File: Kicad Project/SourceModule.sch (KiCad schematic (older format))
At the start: 0 parts

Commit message: Damian edits
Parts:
- added MS?: PowerDivider, symbol PowerDivider
- added U?: RMK-3-93+, symbol RMK-3-93+
- added VCO?: MAX2752, symbol MAX2752
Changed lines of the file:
@@
 $Descr A4 11693 8268
 encoding utf-8
-Sheet 2 3
+Sheet 2 4
 Title ""
 Date ""
@@
 Comment4 ""
 $EndDescr
+$Comp
+L MAX2752 VCO?
+U 1 1 59F141B1
+P 3700 2450
+F 0 "VCO?" H 4100 3000 60  0000 C CNN
+F 1 "MAX2752" H 3400 3000 60  0000 C CNN
+F 2 "" H 3700 2450 60  0001 C CNN
+F 3 "" H 3700 2450 60  0001 C CNN
+	1    3700 2450
+	1    0    0    -1
+$EndComp
+$Comp
+L RMK-3-93+ U?
+U 1 1 59F14344
+P 5750 2250
+F 0 "U?" H 6190 2820 60  0000 C CNN
+F 1 "RMK-3-93+" H 5520 2820 60  0000 C CNN
+F 2 "" H 5750 2250 60  0001 C CNN
+F 3 "" H 5750 2250 60  0001 C CNN
+	1    5750 2250
+	1    0    0    -1
+$EndComp
+$Comp
+L PowerDivider MS?
+U 1 1 59F143BD
+P 7600 2250
+F 0 "MS?" H 8010 2800 60  0000 C CNN
+F 1 "PowerDivider" H 7390 2800 60  0000 C CNN
+F 2 "" H 7600 2250 60  0001 C CNN
+F 3 "" H 7600 2250 60  0001 C CNN
+	1    7600 2250
+	1    0    0    -1
+$EndComp
 $EndSCHEMATC

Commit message: Component Library linked Circuit work on Source Module
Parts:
- added C? (x2): 220pF, symbol C
- added C?: .1uF, symbol C
- added C?: C, symbol C
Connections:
- net labels added: +3.3V, GND
- wire segments 0 -> 22
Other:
- note added: "-3dBm"
- note added: "0dBm\n"
- note added: "Amplifier"
- note added: "Frequency Feedback"
- note added: "Frequency Multiplier"
- note added: "Power Splitter"
- note added: "Teensy Interface"
- note added: "To Premp\nFrequency Multiplier"
- note added: "To TX/RX multiplier"
- note added: "Voltage Controlled Oscillator\n"
- moved on the sheet: MS?, U?, VCO?
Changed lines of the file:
@@
 LIBS:contrib
 LIBS:valves
+LIBS:RadarProject
 LIBS:Radar-cache
 EELAYER 25 0
@@
 L MAX2752 VCO?
 U 1 1 59F141B1
-P 3700 2450
-F 0 "VCO?" H 4100 3000 60  0000 C CNN
-F 1 "MAX2752" H 3400 3000 60  0000 C CNN
-F 2 "" H 3700 2450 60  0001 C CNN
-F 3 "" H 3700 2450 60  0001 C CNN
-	1    3700 2450
+P 2900 2450
+F 0 "VCO?" H 3300 3000 60  0000 C CNN
+F 1 "MAX2752" H 2600 3000 60  0000 C CNN
+F 2 "" H 2900 2450 60  0001 C CNN
+F 3 "" H 2900 2450 60  0001 C CNN
+	1    2900 2450
 	1    0    0    -1
 $EndComp
@@
 L RMK-3-93+ U?
 U 1 1 59F14344
-P 5750 2250
-F 0 "U?" H 6190 2820 60  0000 C CNN
-F 1 "RMK-3-93+" H 5520 2820 60  0000 C CNN
-F 2 "" H 5750 2250 60  0001 C CNN
-F 3 "" H 5750 2250 60  0001 C CNN
-	1    5750 2250
+P 6850 2250
+F 0 "U?" H 7290 2820 60  0000 C CNN
+F 1 "RMK-3-93+" H 6620 2820 60  0000 C CNN
+F 2 "" H 6850 2250 60  0001 C CNN
+F 3 "" H 6850 2250 60  0001 C CNN
+	1    6850 2250
 	1    0    0    -1
 $EndComp
@@
 L PowerDivider MS?
 U 1 1 59F143BD
-P 7600 2250
-F 0 "MS?" H 8010 2800 60  0000 C CNN
-F 1 "PowerDivider" H 7390 2800 60  0000 C CNN
-F 2 "" H 7600 2250 60  0001 C CNN
-F 3 "" H 7600 2250 60  0001 C CNN
-	1    7600 2250
-	1    0    0    -1
-$EndComp
+P 9000 2300
+F 0 "MS?" H 9410 2850 60  0000 C CNN
+F 1 "PowerDivider" H 8790 2850 60  0000 C CNN
+F 2 "" H 9000 2300 60  0001 C CNN
+F 3 "" H 9000 2300 60  0001 C CNN
+	1    9000 2300
+	1    0    0    -1
+$EndComp
+$Comp
+L +3.3V #PWR?
+U 1 1 59F4A689
+P 4100 2600
+F 0 "#PWR?" H 4100 2450 50  0001 C CNN
+F 1 "+3.3V" H 4100 2740 50  0000 C CNN
+F 2 "" H 4100 2600 50  0001 C CNN
+F 3 "" H 4100 2600 50  0001 C CNN
+	1    4100 2600
+	1    0    0    -1
+$EndComp
+Wire Wire Line
+	3600 2650 4100 2650
+Wire Wire Line
+	4100 2650 4300 2650
+Wire Wire Line
+	4100 2850 4100 2650
+Wire Wire Line
+	4100 2650 4100 2600
+Wire Wire Line
+	3600 2850 3900 2850
+Wire Wire Line
+	3900 2850 4100 2850
+Connection ~ 4100 2650
+$Comp
+L C C?
+U 1 1 59F4A7A6
+P 3900 3150
+F 0 "C?" H 3925 3250 50  0000 L CNN
+F 1 "220pF" H 3925 3050 50  0000 L CNN
+F 2 "" H 3938 3000 50  0001 C CNN
+F 3 "" H 3900 3150 50  0001 C CNN
+	1    3900 3150
+	1    0    0    -1
+$EndComp
+$Comp
+L C C?
+U 1 1 59F4A7E2
+P 4300 2850
+F 0 "C?" H 4325 2950 50  0000 L CNN
+F 1 "220pF" H 4325 2750 50  0000 L CNN
+F 2 "" H 4338 2700 50  0001 C CNN
+F 3 "" H 4300 2850 50  0001 C CNN
+	1    4300 2850
+	1    0    0    -1
+$EndComp
+$Comp
+L C C?
+U 1 1 59F4A91F
+P 1750 1700
+F 0 "C?" H 1775 1800 50  0000 L CNN
+F 1 ".1uF" H 1775 1600 50  0000 L CNN
+F 2 "" H 1788 1550 50  0001 C CNN
+F 3 "" H 1750 1700 50  0001 C CNN
+	1    1750 1700
+	1    0    0    -1
+$EndComp
+$Comp
+L GND #PWR?
+U 1 1 59F4A990
+P 1750 1850
+F 0 "#PWR?" H 1750 1600 50  0001 C CNN
+F 1 "GND" H 1750 1700 50  0000 C CNN
+F 2 "" H 1750 1850 50  0001 C CNN
+F 3 "" H 1750 1850 50  0001 C CNN
+	1    1750 1850
+	1    0    0    -1
+$EndComp
+$Comp
+L GND #PWR?
+U 1 1 59F4AA4C
+P 3900 3300
+F 0 "#PWR?" H 3900 3050 50  0001 C CNN
+F 1 "GND" H 3900 3150 50  0000 C CNN
+F 2 "" H 3900 3300 50  0001 C CNN
+F 3 "" H 3900 3300 50  0001 C CNN
+	1    3900 3300
+	1    0    0    -1
+$EndComp
+$Comp
+L GND #PWR?
+U 1 1 59F4AA6C
+P 4300 3000
+F 0 "#PWR?" H 4300 2750 50  0001 C CNN
+F 1 "GND" H 4300 2850 50  0000 C CNN
+F 2 "" H 4300 3000 50  0001 C CNN
+F 3 "" H 4300 3000 50  0001 C CNN
+	1    4300 3000
+	1    0    0    -1
+$EndComp
+Wire Wire Line
+	3900 2850 3900 3000
+Connection ~ 3900 2850
+Wire Wire Line
+	4300 2650 4300 2700
+$Comp
+L GND #PWR?
+U 1 1 59F4AB52
+P 3850 1750
+F 0 "#PWR?" H 3850 1500 50  0001 C CNN
+F 1 "GND" H 3850 1600 50  0000 C CNN
+F 2 "" H 3850 1750 50  0001 C CNN
+F 3 "" H 3850 1750 50  0001 C CNN
+	1    3850 1750
+	1    0    0    -1
+$EndComp
+Wire Wire Line
+	3600 2050 3700 2050
+Wire Wire Line
+	3700 2050 3700 1600
+Wire Wire Line
+	3700 1600 3850 1600
+Wire Wire Line
+	3850 1600 3850 1750
+Wire Wire Line
+	2200 2050 2200 1400
+Wire Wire Line
+	2200 1400 1750 1400
+Wire Wire Line
+	1750 1400 1750 1550
+Wire Wire Line
+	2200 2250 1700 2250
+Wire Wire Line
+	3600 2250 4050 2250
+$Comp
+L C C?
+U 1 1 59F4AD70
+P 4200 2250
+F 0 "C?" H 4225 2350 50  0000 L CNN
+F 1 "C" H 4225 2150 50  0000 L CNN
+F 2 "" H 4238 2100 50  0001 C CNN
+F 3 "" H 4200 2250 50  0001 C CNN
+	1    4200 2250
+	0    1    1    0
+$EndComp
+$Comp
+L GND #PWR?
+U 1 1 59F4AE46
+P 1550 2700
+F 0 "#PWR?" H 1550 2450 50  0001 C CNN
+F 1 "GND" H 1550 2550 50  0000 C CNN
+F 2 "" H 1550 2700 50  0001 C CNN
+F 3 "" H 1550 2700 50  0001 C CNN
+	1    1550 2700
+	1    0    0    -1
+$EndComp
+Wire Wire Line
+	1550 2700 1550 2650
+Wire Wire Line
+	1550 2650 2200 2650
+Text Notes 650  1700 0    60   ~ 0
+Teensy Interface
+Text Notes 2450 1150 0    60   ~ 0
+Voltage Controlled Oscillator\n
+Text Notes 5050 1750 0    60   ~ 0
+Amplifier
+Text Notes 6350 1400 0    60   ~ 0
+Frequency Multiplier
+Text Notes 8600 1600 0    60   ~ 0
+Power Splitter
+Text Notes 9600 2450 0    60   ~ 0
+To Premp\nFrequency Multiplier
+Text Notes 9650 1900 0    60   ~ 0
+To TX/RX multiplier
+Wire Wire Line
+	4350 2250 5150 2250
+Wire Wire Line
+	5150 2250 5150 3700
+Wire Wire Line
+	5150 3700 1700 3700
+Text Notes 1900 3650 0    60   ~ 0
+Frequency Feedback
+$Comp
+L GND #PWR?
+U 1 1 59F4B365
+P 6850 2850
+F 0 "#PWR?" H 6850 2600 50  0001 C CNN
+F 1 "GND" H 6850 2700 50  0000 C CNN
+F 2 "" H 6850 2850 50  0001 C CNN
+F 3 "" H 6850 2850 50  0001 C CNN
+	1    6850 2850
+	1    0    0    -1
+$EndComp
+Text Notes 10700 1600 0    60   ~ 0
+0dBm\n
+Connection ~ 5150 2250
+Text Notes 4450 2200 0    60   ~ 0
+-3dBm
 $EndSCHEMATC

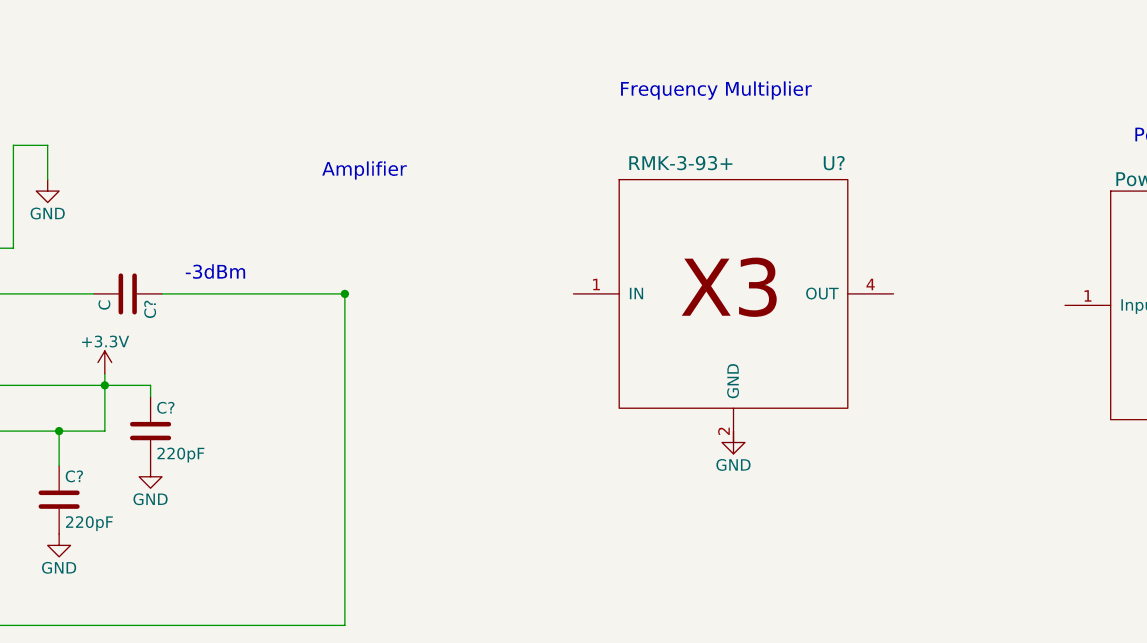
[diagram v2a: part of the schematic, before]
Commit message: Added Power calculations and resistive divider
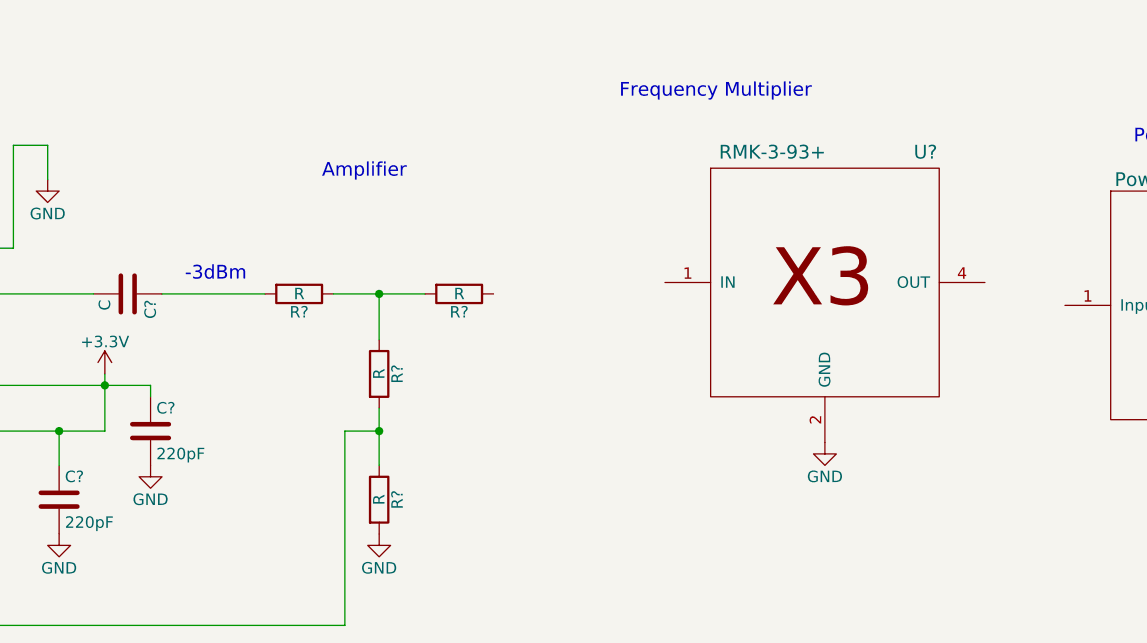
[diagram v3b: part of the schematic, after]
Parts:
- added R? (x4): R, symbol R
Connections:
- wire segments 22 -> 28
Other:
- moved on the sheet: U?
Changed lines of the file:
@@
 L RMK-3-93+ U?
 U 1 1 59F14344
-P 6850 2250
-F 0 "U?" H 7290 2820 60  0000 C CNN
-F 1 "RMK-3-93+" H 6620 2820 60  0000 C CNN
-F 2 "" H 6850 2250 60  0001 C CNN
-F 3 "" H 6850 2250 60  0001 C CNN
-	1    6850 2250
+P 7250 2200
+F 0 "U?" H 7690 2770 60  0000 C CNN
+F 1 "RMK-3-93+" H 7020 2770 60  0000 C CNN
+F 2 "" H 7250 2200 60  0001 C CNN
+F 3 "" H 7250 2200 60  0001 C CNN
+	1    7250 2200
 	1    0    0    -1
 $EndComp
@@
 To TX/RX multiplier
 Wire Wire Line
-	4350 2250 5150 2250
-Wire Wire Line
-	5150 2250 5150 3700
-Wire Wire Line
 	5150 3700 1700 3700
 Text Notes 1900 3650 0    60   ~ 0
@@
 L GND #PWR?
 U 1 1 59F4B365
-P 6850 2850
-F 0 "#PWR?" H 6850 2600 50  0001 C CNN
-F 1 "GND" H 6850 2700 50  0000 C CNN
-F 2 "" H 6850 2850 50  0001 C CNN
-F 3 "" H 6850 2850 50  0001 C CNN
-	1    6850 2850
+P 7250 2900
+F 0 "#PWR?" H 7250 2650 50  0001 C CNN
+F 1 "GND" H 7250 2750 50  0000 C CNN
+F 2 "" H 7250 2900 50  0001 C CNN
+F 3 "" H 7250 2900 50  0001 C CNN
+	1    7250 2900
 	1    0    0    -1
 $EndComp
 Text Notes 10700 1600 0    60   ~ 0
 0dBm\n
-Connection ~ 5150 2250
 Text Notes 4450 2200 0    60   ~ 0
 -3dBm
+$Comp
+L R R?
+U 1 1 59F79D10
+P 4950 2250
+F 0 "R?" V 5030 2250 50  0000 C CNN
+F 1 "R" V 4950 2250 50  0000 C CNN
+F 2 "" V 4880 2250 50  0001 C CNN
+F 3 "" H 4950 2250 50  0001 C CNN
+	1    4950 2250
+	0    1    1    0
+$EndComp
+$Comp
+L R R?
+U 1 1 59F79D75
+P 5300 2600
+F 0 "R?" V 5380 2600 50  0000 C CNN
+F 1 "R" V 5300 2600 50  0000 C CNN
+F 2 "" V 5230 2600 50  0001 C CNN
+F 3 "" H 5300 2600 50  0001 C CNN
+	1    5300 2600
+	1    0    0    -1
+$EndComp
+$Comp
+L R R?
+U 1 1 59F79DA8
+P 5650 2250
+F 0 "R?" V 5730 2250 50  0000 C CNN
+F 1 "R" V 5650 2250 50  0000 C CNN
+F 2 "" V 5580 2250 50  0001 C CNN
+F 3 "" H 5650 2250 50  0001 C CNN
+	1    5650 2250
+	0    1    1    0
+$EndComp
+$Comp
+L R R?
+U 1 1 59F7A0A9
+P 5300 3150
+F 0 "R?" V 5380 3150 50  0000 C CNN
+F 1 "R" V 5300 3150 50  0000 C CNN
+F 2 "" V 5230 3150 50  0001 C CNN
+F 3 "" H 5300 3150 50  0001 C CNN
+	1    5300 3150
+	1    0    0    -1
+$EndComp
+Wire Wire Line
+	5150 2850 5150 3700
+Wire Wire Line
+	5300 2750 5300 2850
+Wire Wire Line
+	5300 2850 5300 3000
+Wire Wire Line
+	5300 2850 5150 2850
+Connection ~ 5300 2850
+$Comp
+L GND #PWR?
+U 1 1 59F7A17E
+P 5300 3300
+F 0 "#PWR?" H 5300 3050 50  0001 C CNN
+F 1 "GND" H 5300 3150 50  0000 C CNN
+F 2 "" H 5300 3300 50  0001 C CNN
+F 3 "" H 5300 3300 50  0001 C CNN
+	1    5300 3300
+	1    0    0    -1
+$EndComp
+Wire Wire Line
+	5100 2250 5300 2250
+Wire Wire Line
+	5300 2250 5500 2250
+Wire Wire Line
+	5300 2450 5300 2250
+Connection ~ 5300 2250
+Wire Wire Line
+	4350 2250 4800 2250
 $EndSCHEMATC

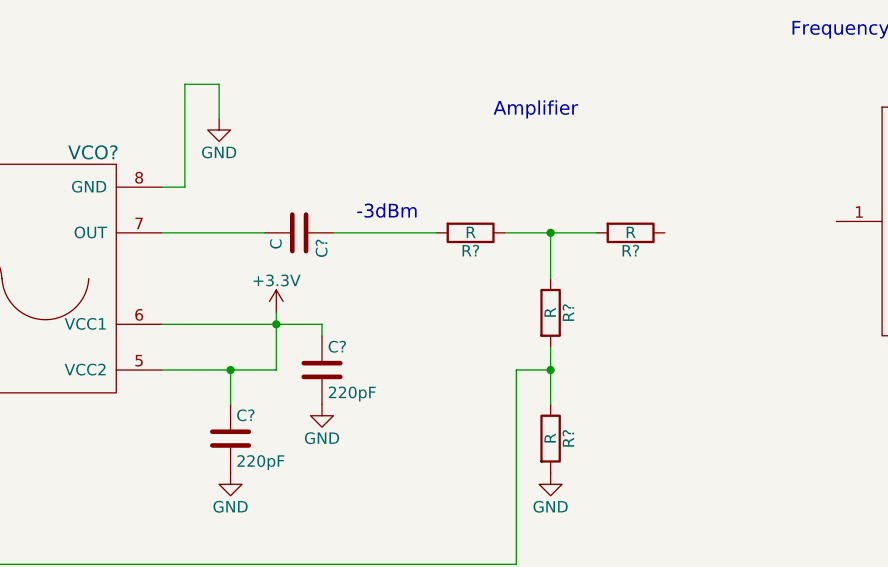
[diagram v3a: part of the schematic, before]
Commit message: Updated labels
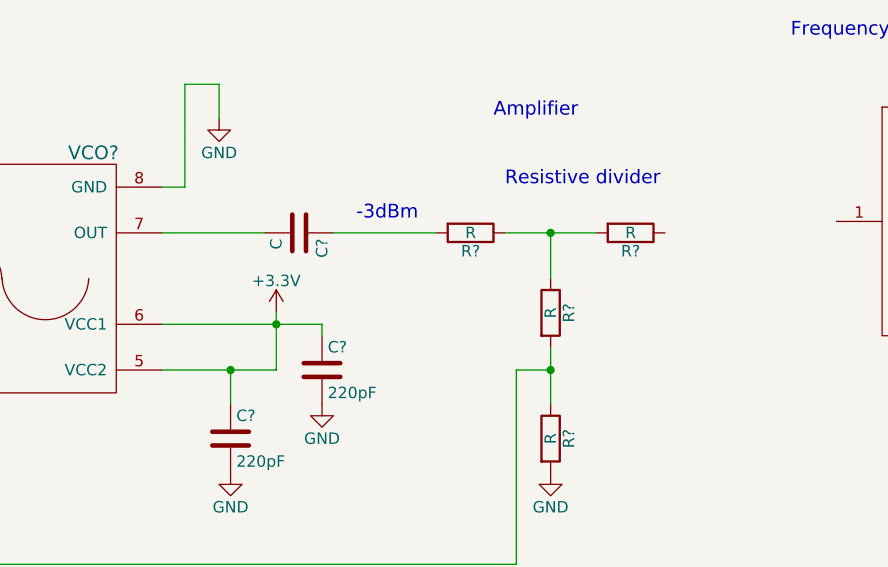
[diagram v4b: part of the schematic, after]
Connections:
- wire segments 28 -> 23
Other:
- note added: "Resistive divider"
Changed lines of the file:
@@
 $EndComp
 Wire Wire Line
-	3600 2650 4100 2650
-Wire Wire Line
-	4100 2650 4300 2650
-Wire Wire Line
-	4100 2850 4100 2650
-Wire Wire Line
-	4100 2650 4100 2600
-Wire Wire Line
-	3600 2850 3900 2850
-Wire Wire Line
-	3900 2850 4100 2850
+	3600 2650 4300 2650
+Wire Wire Line
+	4100 2850 4100 2600
+Wire Wire Line
+	3600 2850 4100 2850
 Connection ~ 4100 2650
 $Comp
@@
 	5150 2850 5150 3700
 Wire Wire Line
-	5300 2750 5300 2850
-Wire Wire Line
-	5300 2850 5300 3000
+	5300 2750 5300 3000
 Wire Wire Line
 	5300 2850 5150 2850
@@
 $EndComp
 Wire Wire Line
-	5100 2250 5300 2250
-Wire Wire Line
-	5300 2250 5500 2250
+	5100 2250 5500 2250
 Wire Wire Line
 	5300 2450 5300 2250
@@
 Wire Wire Line
 	4350 2250 4800 2250
+Text Notes 5100 2050 0    60   ~ 0
+Resistive divider
 $EndSCHEMATC

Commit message: Messed with parts
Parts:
- gave numbers to parts that had none: 1
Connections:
- wire segments 23 -> 24
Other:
- note added: "Teensy Control"
- note removed: "Teensy Interface"
- moved on the sheet: .1uF, C?, MS?, R?, U?, VCO?

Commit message: updates
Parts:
- added .1uF, .1uF? (x2), C? (x2): C, symbol C
- added R? (x4): 75, symbol R
- added U? (x2): GALI-2+, symbol GALI-2+
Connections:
- net labels added: +9V
- wire segments 24 -> 43
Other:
- note added: "4 dBM\n"
- note added: "Filter?\n"
- note added: "lamda/4\n"
- moved on the sheet: .1uF, MS?

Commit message: PCB Changes
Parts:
- .1uF1, .1uF2: renamed from .1uF; footprint (none) -> Capacitors_SMD:C_0603
- .1uF3, .1uF4: renamed from .1uF?; footprint (none) -> Capacitors_SMD:C_0603
- C5, C6, C7, C8, C9: renamed from C?; footprint (none) -> Capacitors_SMD:C_0603
- R10, R11, R12, R13, R14, R7, R8, R9: renamed from R?; footprint (none) -> Resistors_SMD:R_0603
- U6, U8: renamed from U?; footprint (none) -> RadarComponents:Amplifier
- gave numbers to parts that had none: 3

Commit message: PCB and Schematic updates
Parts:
- .1uF1, .1uF2, .1uF3, .1uF4, C5, C6, C7, C8, C9: footprint Capacitors_SMD:C_0603 -> RadarComponents:100PAD
- R10, R11, R12, R13, R14, R7, R8, R9: footprint Resistors_SMD:R_0603 -> RadarComponents:100PAD
- U7: footprint (none) -> RadarComponents:TT1224
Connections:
- net labels added: PowerSplitter
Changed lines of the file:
@@
 F 0 "U7" H 7740 2770 60  0000 C CNN
 F 1 "RMK-3-93+" H 7070 2770 60  0000 C CNN
-F 2 "" H 7300 2200 60  0001 C CNN
+F 2 "RadarComponents:TT1224" H 7300 2200 60  0001 C CNN
 F 3 "" H 7300 2200 60  0001 C CNN
 	1    7300 2200
@@
 F 0 "C6" H 3225 3200 50  0000 L CNN
 F 1 "220pF" H 3225 3000 50  0000 L CNN
-F 2 "Capacitors_SMD:C_0603" H 3238 2950 50  0001 C CNN
+F 2 "RadarComponents:100PAD" H 3238 2950 50  0001 C CNN
 F 3 "" H 3200 3100 50  0001 C CNN
 	1    3200 3100
@@
 F 0 "C7" H 3625 3200 50  0000 L CNN
 F 1 "220pF" H 3625 3000 50  0000 L CNN
-F 2 "Capacitors_SMD:C_0603" H 3638 2950 50  0001 C CNN
+F 2 "RadarComponents:100PAD" H 3638 2950 50  0001 C CNN
 F 3 "" H 3600 3100 50  0001 C CNN
 	1    3600 3100
@@
 F 0 "C5" H 1075 1750 50  0000 L CNN
 F 1 ".1uF" H 1075 1550 50  0000 L CNN
-F 2 "Capacitors_SMD:C_0603" H 1088 1500 50  0001 C CNN
+F 2 "RadarComponents:100PAD" H 1088 1500 50  0001 C CNN
 F 3 "" H 1050 1650 50  0001 C CNN
 	1    1050 1650
@@
 F 0 ".1uF1" H 3425 2300 50  0000 L CNN
 F 1 "C" H 3425 2100 50  0000 L CNN
-F 2 "Capacitors_SMD:C_0603" H 3438 2050 50  0001 C CNN
+F 2 "RadarComponents:100PAD" H 3438 2050 50  0001 C CNN
 F 3 "" H 3400 2200 50  0001 C CNN
 	1    3400 2200
@@
 F 0 "R9" V 5730 2200 50  0000 C CNN
 F 1 "R" V 5650 2200 50  0000 C CNN
-F 2 "Resistors_SMD:R_0603" V 5580 2200 50  0001 C CNN
+F 2 "RadarComponents:100PAD" V 5580 2200 50  0001 C CNN
 F 3 "" H 5650 2200 50  0001 C CNN
 	1    5650 2200
@@
 F 0 "R10" V 6080 2550 50  0000 C CNN
 F 1 "R" V 6000 2550 50  0000 C CNN
-F 2 "Resistors_SMD:R_0603" V 5930 2550 50  0001 C CNN
+F 2 "RadarComponents:100PAD" V 5930 2550 50  0001 C CNN
 F 3 "" H 6000 2550 50  0001 C CNN
 	1    6000 2550
@@
 F 0 "R12" V 6430 2200 50  0000 C CNN
 F 1 "R" V 6350 2200 50  0000 C CNN
-F 2 "Resistors_SMD:R_0603" V 6280 2200 50  0001 C CNN
+F 2 "RadarComponents:100PAD" V 6280 2200 50  0001 C CNN
 F 3 "" H 6350 2200 50  0001 C CNN
 	1    6350 2200
@@
 F 0 "R11" V 6080 3100 50  0000 C CNN
 F 1 "R" V 6000 3100 50  0000 C CNN
-F 2 "Resistors_SMD:R_0603" V 5930 3100 50  0001 C CNN
+F 2 "RadarComponents:100PAD" V 5930 3100 50  0001 C CNN
 F 3 "" H 6000 3100 50  0001 C CNN
 	1    6000 3100
@@
 F 0 ".1uF2" H 5375 2300 50  0000 L CNN
 F 1 "C" H 5375 2100 50  0000 L CNN
-F 2 "Capacitors_SMD:C_0603" H 5388 2050 50  0001 C CNN
+F 2 "RadarComponents:100PAD" H 5388 2050 50  0001 C CNN
 F 3 "" H 5350 2200 50  0001 C CNN
 	1    5350 2200
@@
 F 0 "R8" V 5480 1300 50  0000 C CNN
 F 1 "75" V 5400 1300 50  0000 C CNN
-F 2 "Resistors_SMD:R_0603" V 5330 1300 50  0001 C CNN
+F 2 "RadarComponents:100PAD" V 5330 1300 50  0001 C CNN
 F 3 "" H 5400 1300 50  0001 C CNN
 	1    5400 1300
@@
 F 0 "C8" H 5325 1800 50  0000 L CNN
 F 1 "C" H 5325 1600 50  0000 L CNN
-F 2 "Capacitors_SMD:C_0603" H 5338 1550 50  0001 C CNN
+F 2 "RadarComponents:100PAD" H 5338 1550 50  0001 C CNN
 F 3 "" H 5300 1700 50  0001 C CNN
 	1    5300 1700
@@
 F 0 "R14" V 10030 1300 50  0000 C CNN
 F 1 "75" V 9950 1300 50  0000 C CNN
-F 2 "Resistors_SMD:R_0603" V 9880 1300 50  0001 C CNN
+F 2 "RadarComponents:100PAD" V 9880 1300 50  0001 C CNN
 F 3 "" H 9950 1300 50  0001 C CNN
 	1    9950 1300
@@
 F 0 "C9" H 9875 1800 50  0000 L CNN
 F 1 "C" H 9875 1600 50  0000 L CNN
-F 2 "Capacitors_SMD:C_0603" H 9888 1550 50  0001 C CNN
+F 2 "RadarComponents:100PAD" H 9888 1550 50  0001 C CNN
 F 3 "" H 9850 1700 50  0001 C CNN
 	1    9850 1700
@@
 F 0 ".1uF3" H 8175 2300 50  0000 L CNN
 F 1 "C" H 8175 2100 50  0000 L CNN
-F 2 "Capacitors_SMD:C_0603" H 8188 2050 50  0001 C CNN
+F 2 "RadarComponents:100PAD" H 8188 2050 50  0001 C CNN
 F 3 "" H 8150 2200 50  0001 C CNN
 	1    8150 2200
@@
 F 0 ".1uF4" H 10075 2300 50  0000 L CNN
 F 1 "C" H 10075 2100 50  0000 L CNN
-F 2 "Capacitors_SMD:C_0603" H 10088 2050 50  0001 C CNN
+F 2 "RadarComponents:100PAD" H 10088 2050 50  0001 C CNN
 F 3 "" H 10050 2200 50  0001 C CNN
 	1    10050 2200
@@
 F 0 "R7" V 5230 2050 50  0000 C CNN
 F 1 "75" V 5150 2050 50  0000 C CNN
-F 2 "Resistors_SMD:R_0603" V 5080 2050 50  0001 C CNN
+F 2 "RadarComponents:100PAD" V 5080 2050 50  0001 C CNN
 F 3 "" H 5150 2050 50  0001 C CNN
 	1    5150 2050
@@
 F 0 "R13" V 9780 2050 50  0000 C CNN
 F 1 "75" V 9700 2050 50  0000 C CNN
-F 2 "Resistors_SMD:R_0603" V 9630 2050 50  0001 C CNN
+F 2 "RadarComponents:100PAD" V 9630 2050 50  0001 C CNN
 F 3 "" H 9700 2050 50  0001 C CNN
 	1    9700 2050
@@
 Wire Wire Line
 	9700 1300 9700 1900
+Text Label 9250 3950 0    60   ~ 0
+PowerSplitter
 $EndSCHEMATC
